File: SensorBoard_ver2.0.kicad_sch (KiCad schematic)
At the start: 0 parts

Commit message: 回路図作成
まだまだかかる
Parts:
- added C10, C7, C8, C9: 0.1μF, Capacitor_SMD:C_0603_1608Metric, symbol Device:C
- added D? (x4): LED, LED_SMD:LED_0603_1608Metric, symbol Device:LED
- added J? (x2): CANConn, Connector_JST:JST_XA_S04B-XASK-1_1x04_P2.50mm_Horizontal, symbol Connector:Conn_01x04_Socket
- added R? (x4): 10kΩ, Resistor_SMD:R_0603_1608Metric, symbol Device:R
- added SW2: 12V⇔5V Change, Connector_PinHeader_2.54mm:PinHeader_1x03_P2.54mm_Vertical, symbol Switch:SW_Nidec_CAS-120A1
- added U2: L7805, Package_TO_SOT_SMD:TO-252-2, symbol Regulator_Linear:L7805
- added U3: 3.3V Regulator, Package_TO_SOT_SMD:TO-252-2, symbol Regulator_Linear:L7805
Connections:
- new net: D?.2 (A), R?.2 (x4)
- new net +3.3V: C10.1, R?.1, U3.3 (OUT)
- new net +5V: C9.1, R?.1, SW2.2 (B), U3.1 (IN)
- new net +5VR: C8.1, R?.1, SW2.1 (C), U2.3 (OUT)
- new net CANH: J?.2 (Pin_2), J?.2 (Pin_2)
- new net CANL: J?.3 (Pin_3), J?.3 (Pin_3)
- new net GND: C10.2, C7.2, C8.2, C9.2, D?.1 (K), D?.1 (K), D?.1 (K), D?.1 (K), J?.4 (Pin_4), J?.4 (Pin_4), U2.2 (GND), U3.2 (GND)
- new net VCC: C7.1, J?.1 (Pin_1), J?.1 (Pin_1), R?.1, SW2.3 (A), U2.1 (IN)
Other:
- removed sheet MCU_F303K8T
- added sheet CANUnit (CANUnit.kicad_sch)
- added sheet Enc_Limit_Unit (Sensor.kicad_sch)
- added sheet MCU_Unit (MCU.kicad_sch)
- added sheet RS485_Unit (RS485.kicad_sch)
- note added: "12V → 5V Regulator"
- note added: "5V Select SW"
- note added: "5V → 3.3V Regulator"
- note added: "Indicator LED"
- note added: "PowerOnly Type-C"
- note added: "Power_Unit"

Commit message: 回路図の作成
完成が見えてきた
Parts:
- removed J? (x2): CANConn, Connector_JST:JST_XA_S04B-XASK-1_1x04_P2.50mm_Horizontal, symbol Connector:Conn_01x04_Socket
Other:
- sheet CANUnit ports: added none; removed CANH, CANL
- sheet Enc_Limit_Unit ports: added Limit_Mode; removed Lim_Mode
- sheet MCU_Unit ports: added CTRL, Limit_Mode, UARTRX, UARTTX; removed Lim_Mode
- sheet RS485_Unit ports: added CTRL, UARTRX, UARTTX; removed none

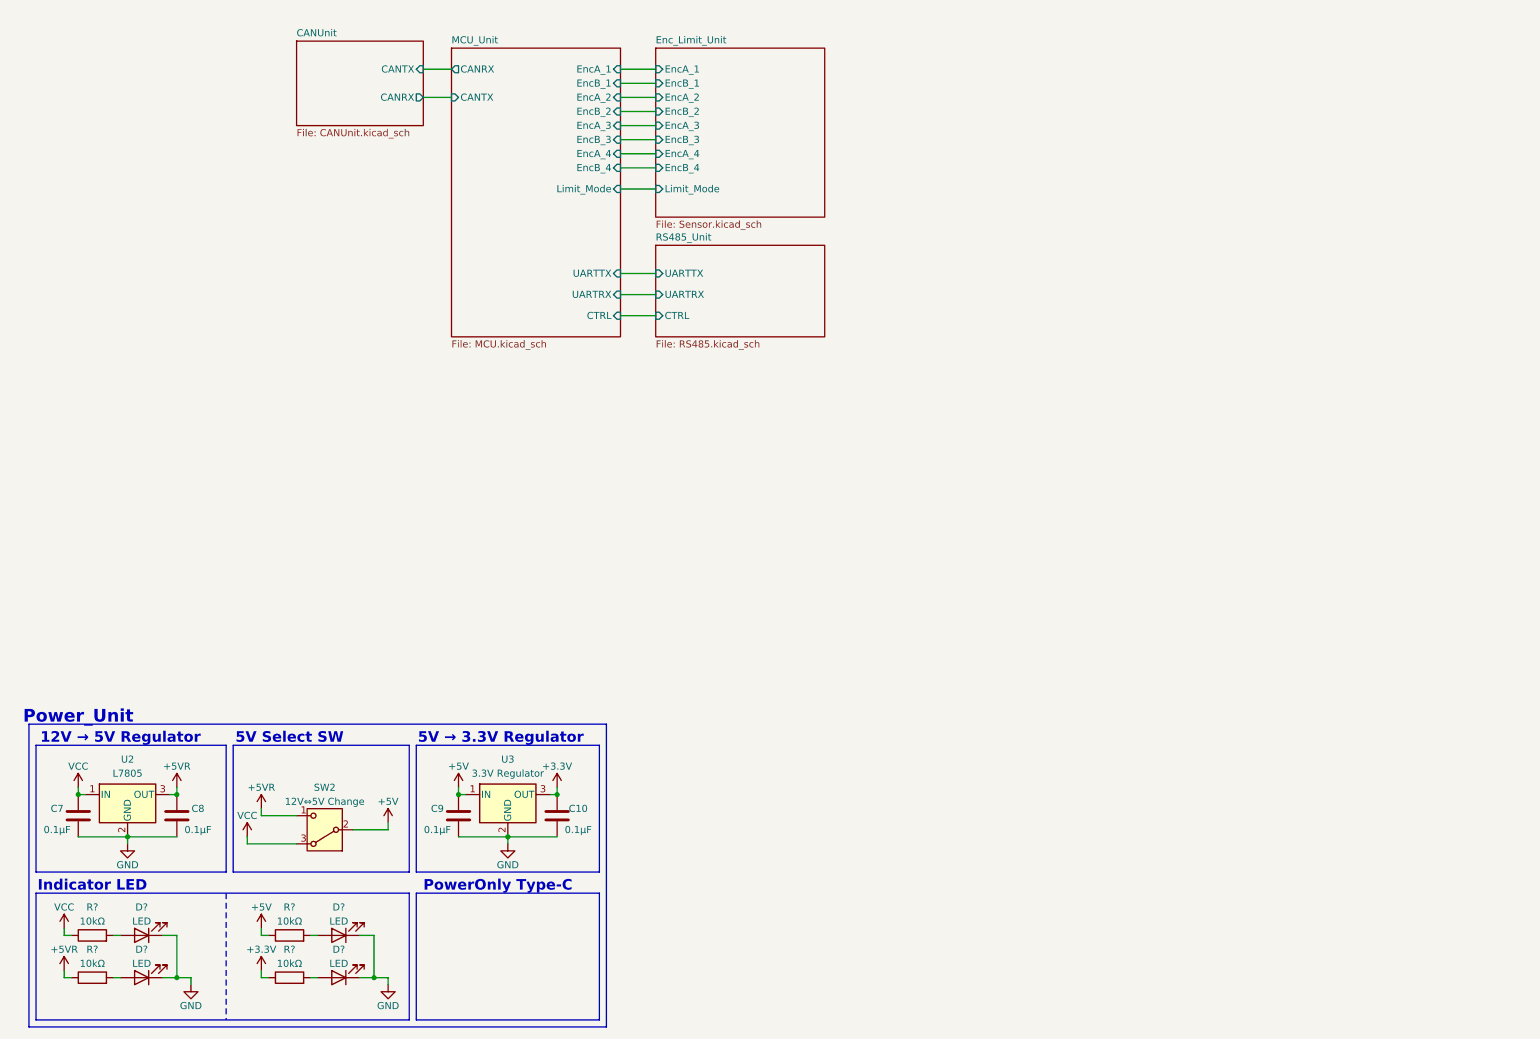
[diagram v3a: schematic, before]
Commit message: 回路図9割完成
回路図は9割完成
次からは配線作業をする
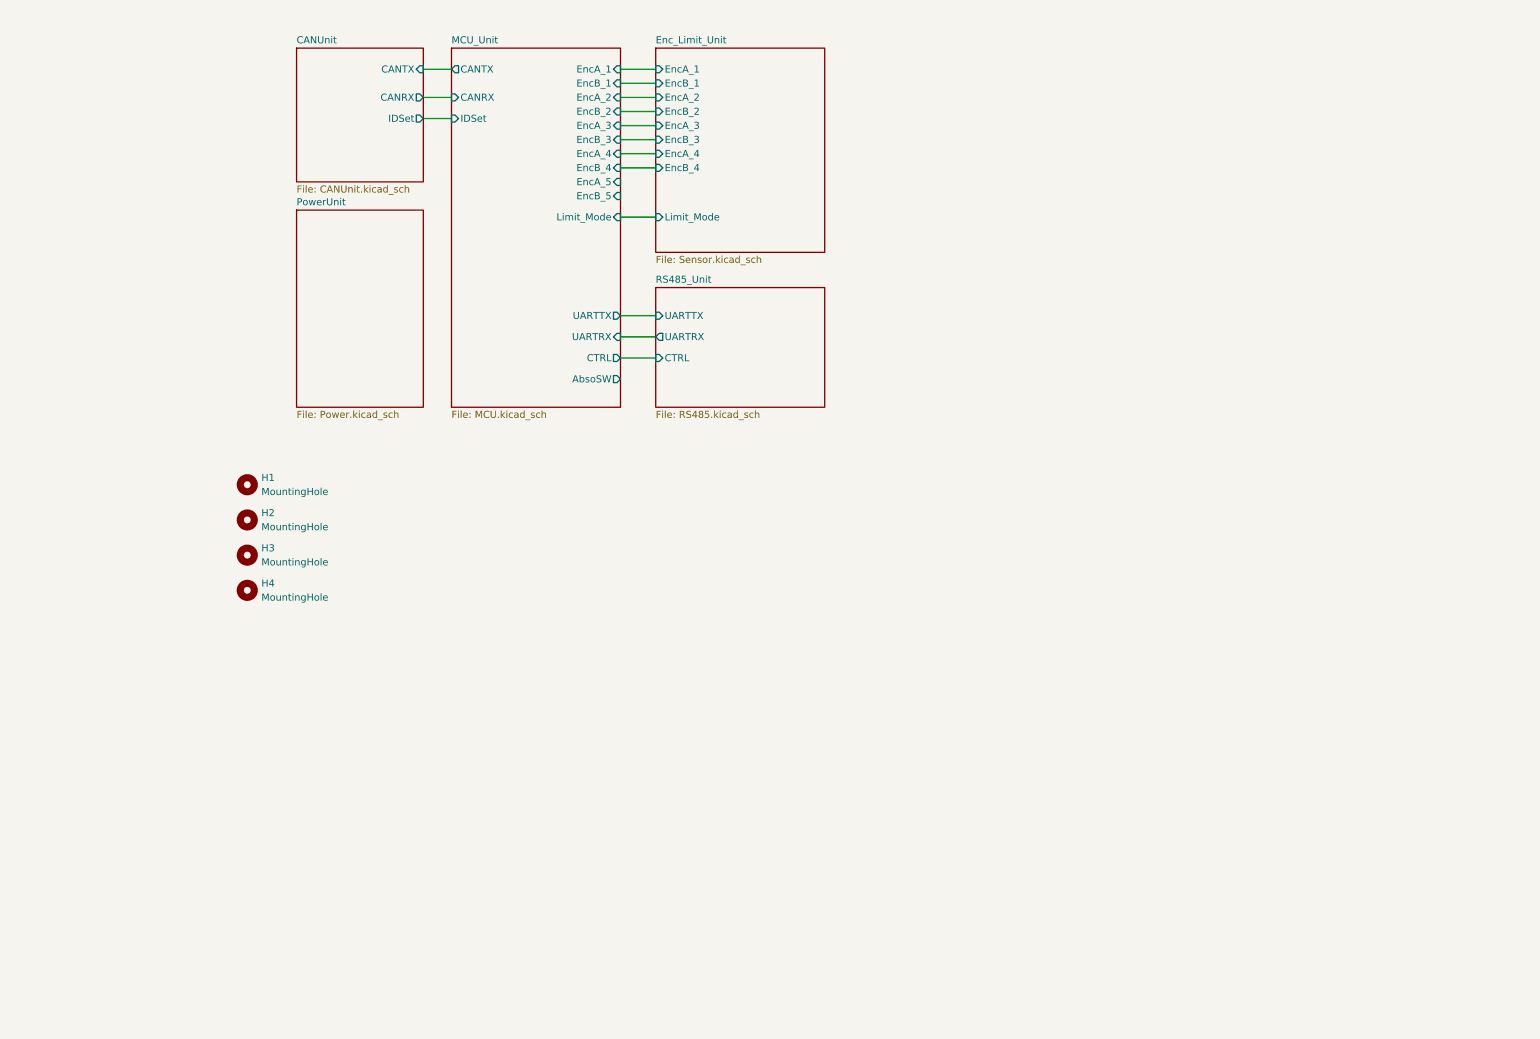
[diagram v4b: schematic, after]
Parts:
- removed C10, C7, C8, C9: 0.1μF, Capacitor_SMD:C_0603_1608Metric, symbol Device:C
- removed D? (x4): LED, LED_SMD:LED_0603_1608Metric, symbol Device:LED
- removed R? (x4): 10kΩ, Resistor_SMD:R_0603_1608Metric, symbol Device:R
- removed SW2: 12V⇔5V Change, Connector_PinHeader_2.54mm:PinHeader_1x03_P2.54mm_Vertical, symbol Switch:SW_Nidec_CAS-120A1
- removed U2: L7805, Package_TO_SOT_SMD:TO-252-2, symbol Regulator_Linear:L7805
- removed U3: 3.3V Regulator, Package_TO_SOT_SMD:TO-252-2, symbol Regulator_Linear:L7805
- added H1, H2, H3, H4: MountingHole, MountingHole:MountingHole_3.2mm_M3_Pad_Via, symbol Mechanical:MountingHole
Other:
- added sheet PowerUnit (Power.kicad_sch)
- sheet CANUnit ports: added IDSet; removed none
- sheet MCU_Unit ports: added AbsoSW, EncA_5, EncB_5, IDSet; removed none
- note removed: "12V → 5V Regulator"
- note removed: "5V Select SW"
- note removed: "5V → 3.3V Regulator"
- note removed: "Indicator LED"
- note removed: "PowerOnly Type-C"
- note removed: "Power_Unit"

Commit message: 回路図作った
リミットとエンコ共存いやかも
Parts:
- added C1, C2, C5, C6: ?, Capacitor_SMD:C_0603_1608Metric, symbol Device:C
- added C10: 1μF, Capacitor_SMD:C_0603_1608Metric, symbol Device:C
- added C11, C12: C, Capacitor_SMD:C_0603_1608Metric, symbol Device:C
- added C13, C3, C4, C7, C8, C9: 0.1μF, Capacitor_SMD:C_0603_1608Metric, symbol Device:C
- added D1, D2, D3: LED, LED_SMD:LED_0603_1608Metric, symbol Device:LED
- added FB1: FerriteBead, Inductor_SMD:L_0603_1608Metric, symbol Device:FerriteBead
- added J1, J2: CANConn, Connector_JST:JST_XA_S04B-XASK-1_1x04_P2.50mm_Horizontal, symbol Connector:Conn_01x04_Socket
- added J10: Limit3-B, Connector_JST:JST_XA_B02B-XASK-1_1x02_P2.50mm_Vertical, symbol Connector:Conn_01x02_Socket
- added J11: USB_C, MyUSB_C:PowerOnlyUSB_C, symbol Connector:Conn_01x02_Socket
- added J12: Limit2-A, Connector_JST:JST_XA_B02B-XASK-1_1x02_P2.50mm_Vertical, symbol Connector:Conn_01x02_Socket
- added J13: Limit2-B, Connector_JST:JST_XA_B02B-XASK-1_1x02_P2.50mm_Vertical, symbol Connector:Conn_01x02_Socket
- added J14: Limit4-A, Connector_JST:JST_XA_B02B-XASK-1_1x02_P2.50mm_Vertical, symbol Connector:Conn_01x02_Socket
- added J15: Limit4-B, Connector_JST:JST_XA_B02B-XASK-1_1x02_P2.50mm_Vertical, symbol Connector:Conn_01x02_Socket
- added J16, J17, J19, J20, J21, J22: Abso, Connector_JST:JST_XA_S04B-XASK-1_1x04_P2.50mm_Horizontal, symbol Connector:Conn_01x04_Socket
- added J18: STLink, Connector_PinHeader_1.27mm:PinHeader_2x07_P1.27mm_Vertical_SMD, symbol Connector_Generic:Conn_02x07_Odd_Even
- added J3: Enc1, Connector_JST:JST_XA_S04B-XASK-1_1x04_P2.50mm_Horizontal, symbol Connector:Conn_01x04_Socket
- added J4: Enc2, Connector_JST:JST_XA_S04B-XASK-1_1x04_P2.50mm_Horizontal, symbol Connector:Conn_01x04_Socket
- added J5: Enc3, Connector_JST:JST_XA_S04B-XASK-1_1x04_P2.50mm_Horizontal, symbol Connector:Conn_01x04_Socket
- added J6: Enc4, Connector_JST:JST_XA_S04B-XASK-1_1x04_P2.50mm_Horizontal, symbol Connector:Conn_01x04_Socket
- added J7: Limit1-A, Connector_JST:JST_XA_B02B-XASK-1_1x02_P2.50mm_Vertical, symbol Connector:Conn_01x02_Socket
- added J8: Limit1-B, Connector_JST:JST_XA_B02B-XASK-1_1x02_P2.50mm_Vertical, symbol Connector:Conn_01x02_Socket
- added J9: Limit3-A, Connector_JST:JST_XA_B02B-XASK-1_1x02_P2.50mm_Vertical, symbol Connector:Conn_01x02_Socket
- added JP1: VCC⇔5V Short, Jumper:SolderJumper-2_P1.3mm_Open_RoundedPad1.0x1.5mm, symbol Jumper:SolderJumper_2_Open
- added R1, R2, R3, R4, R7: 10kΩ, Resistor_SMD:R_0603_1608Metric, symbol Device:R
- added R5: 120Ω, symbol Device:R
- added R6, R8: 120Ω, Resistor_SMD:R_0603_1608Metric, symbol Device:R
- added SW1: CAN_Terminal, Connector_PinHeader_2.54mm:PinHeader_1x03_P2.54mm_Vertical, symbol Switch:SW_Nidec_CAS-120A1
- added SW2: IDSetSW, Connector_PinHeader_2.54mm:PinHeader_1x03_P2.54mm_Vertical, symbol Switch:SW_Nidec_CAS-120A1
- added SW3: Enc⇔Lim Change, Connector_PinHeader_2.54mm:PinHeader_1x03_P2.54mm_Vertical, symbol Switch:SW_Nidec_CAS-120A1
- added SW4: ResetSW, symbol Switch:SW_MEC_5E
- added SW5: RS485_Terminal, Connector_PinHeader_2.54mm:PinHeader_1x03_P2.54mm_Vertical, symbol Switch:SW_Nidec_CAS-120A1
- added SW6: AbsoSW, symbol Switch:SW_MEC_5E
- added U1: L7805, Package_TO_SOT_SMD:TO-252-2, symbol Regulator_Linear:L7805
- added U2: ATA6561, Package_SO:SOIC-8_3.9x4.9mm_P1.27mm, symbol Interface_CAN_LIN:MCP2551-I-SN
- added U3: 3.3V Regulator, Package_TO_SOT_SMD:SOT-223, symbol Regulator_Linear:L7805
- added U4: STM32F303K8Tx, Package_QFP:LQFP-32_7x7mm_P0.8mm, symbol MCU_ST_STM32F3:STM32F303K8Tx
- added U5: MAX3485, Package_SO:SOIC-8_3.9x4.9mm_P1.27mm, symbol Interface_UART:MAX3485
- added Y1: Crystal, Crystal:Crystal_SMD_HC49-SD, symbol Device:Crystal
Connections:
- new net: R8.2, SW5.3 (A)
- new net: D3.2 (A), R3.2
- new net: D2.2 (A), R2.2
- new net: R5.1, SW1.2 (B)
- new net: D1.2 (A), R1.2
- new net: R4.2, U2.8 (STBY)
- new net +3.3V: C10.1, C4.1, C6.1, C7.1, C8.1, FB1.1, J18.3 (Pin_3), R3.1, U2.5 (VIO), U3.3 (OUT), U4.1 (VDD), U4.17 (VDD), U5.8 (VCC)
- new net +3.3VA: FB1.2, U4.5 (VDDA)
- new net +5V: C2.1, C3.1, C5.1, J11.1 (Pin_1), J16.1 (Pin_1), J17.1 (Pin_1), J19.1 (Pin_1), J20.1 (Pin_1), J21.1 (Pin_1), J22.1 (Pin_1), J3.1 (Pin_1), J4.1 (Pin_1), J5.1 (Pin_1), J6.1 (Pin_1), JP1.2 (B), R2.1, U1.3 (OUT), U2.3 (VDD), U3.1 (IN)
- new net AbsoSW: C13.2, SW6.1, SW6.2, U4.27 (PB4)
- new net Booto: R7.1, U4.31 (BOOT0)
- new net CANH: J1.2 (Pin_2), J2.2 (Pin_2), SW1.1 (C), U2.7 (CANH)
- new net CANL: J1.3 (Pin_3), J2.3 (Pin_3), R5.2, U2.6 (CANL)
- new net CANRX: U2.4 (RXD), U4.21 (PA11)
- new net CANTX: U2.1 (TXD), U4.22 (PA12)
- new net CTRL: U4.28 (PB5), U5.2 (~{RE}), U5.3 (DE)
- new net Crystal0: C11.1, U4.2 (PF0), Y1.1
- new net Crystal1: C12.1, U4.3 (PF1), Y1.2
- new net EncA_1: J3.2 (Pin_2), J7.1 (Pin_1), U4.6 (PA0)
- new net EncA_2: J12.1 (Pin_1), J4.2 (Pin_2), U4.10 (PA4)
- new net EncA_3: J5.2 (Pin_2), J9.1 (Pin_1), U4.12 (PA6)
- new net EncA_4: J14.1 (Pin_1), J6.2 (Pin_2), U4.18 (PA8)
- new net EncB_1: J3.3 (Pin_3), J8.1 (Pin_1), U4.7 (PA1)
- new net EncB_2: J13.1 (Pin_1), J4.3 (Pin_3), U4.11 (PA5)
- new net EncB_3: J10.1 (Pin_1), J5.3 (Pin_3), U4.13 (PA7)
- new net EncB_4: J15.1 (Pin_1), J6.3 (Pin_3), U4.19 (PA9)
- new net GND: C1.2, C10.2, C11.2, C12.2, C13.1, C2.2, C3.2, C4.2, C5.2, C6.2, C7.2, C8.2, C9.1, D1.1 (K), D2.1 (K), D3.1 (K), J1.4 (Pin_4), J10.2 (Pin_2), J11.2 (Pin_2), J12.2 (Pin_2), J13.2 (Pin_2), J14.2 (Pin_2), J15.2 (Pin_2), J16.4 (Pin_4), J17.4 (Pin_4), J18.11 (Pin_11), J18.5 (Pin_5), J18.7 (Pin_7), J19.4 (Pin_4), J2.4 (Pin_4), J20.4 (Pin_4), J21.4 (Pin_4), J22.4 (Pin_4), J3.4 (Pin_4), J4.4 (Pin_4), J5.4 (Pin_4), J6.4 (Pin_4), J7.2 (Pin_2), J8.2 (Pin_2), J9.2 (Pin_2), R4.1, R7.2, SW2.2 (B), SW3.2 (B), SW4.3 (K), SW4.4 (A), SW6.3 (K), SW6.4 (A), U1.2 (GND), U2.2 (VSS), U3.2 (GND), U4.16 (VSS), U4.32 (VSS), U5.5 (GND)
- new net IDSet: SW2.1 (C), U4.20 (PA10)
- new net LED1: U4.14 (PB0)
- new net LED2: U4.15 (PB1)
- new net LimitMode: SW3.1 (C), U4.9 (PA3)
- new net NRST: C9.2, J18.12 (Pin_12), SW4.1, SW4.2, U4.4 (NRST)
- new net RS485_A: J16.2 (Pin_2), J17.2 (Pin_2), J19.2 (Pin_2), J21.2 (Pin_2), J22.2 (Pin_2), R6.1, R8.1, U5.6 (A)
- new net RS485_B: J16.3 (Pin_3), J17.3 (Pin_3), J19.3 (Pin_3), J21.3 (Pin_3), J22.3 (Pin_3), R6.2, SW5.2 (B), U5.7 (B)
- new net SWCLK: J18.6 (Pin_6), U4.24 (PA14)
- new net SWDIO: J18.4 (Pin_4), U4.23 (PA13)
- new net UARTRX: U5.1 (RO)
- new net UARTTX: U4.29 (PB6), U4.30 (PB7), U5.4 (DI)
- new net VCC: C1.1, J1.1 (Pin_1), J2.1 (Pin_1), JP1.1 (A), R1.1, U1.1 (IN)
- new net VCPRX: J18.13 (Pin_13), J20.3 (Pin_3), U4.25 (PA15)
- new net VCPTX: J18.14 (Pin_14), J20.2 (Pin_2), U4.8 (PA2)
- no-connect marks 0 -> 5
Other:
- removed sheet CANUnit
- removed sheet Enc_Limit_Unit
- removed sheet MCU_Unit
- removed sheet PowerUnit
- removed sheet RS485_Unit
- note added: "12V → 5V Regulator"
- note added: "5V Select SW"
- note added: "5V → 3.3V Regulator"
- note added: "ATA6561"
- note added: "AbsoSW"
- note added: "CAN_Terminal"
- note added: "CAN_Unit"
- note added: "Crystal"
- note added: "Decoupling Capacitor"
- note added: "Encorder_Pin"
- note added: "Enc⇔Limit Change"
- note added: "F303K8T"
- note added: "IDSet_SW"
- note added: "Indicator LED"
- note added: "Limit_Pin"
- note added: "MCU_Unit"
- note added: "PowerOnly Type-C"
- note added: "Power_Unit"
- note added: "RS485_Unit"
- note added: "Reset & Booto"
- note added: "STLink"
- note added: "Sensor_Unit"
- title: (none) -> SensorBoard(Potato)_ver2.0
- moved on the sheet: H1, H2, H3, H4
